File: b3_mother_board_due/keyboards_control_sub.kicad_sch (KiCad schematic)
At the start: 20 parts, among them J14 Upper Keyboard Left, J15 Upper Keyboard Right, J16 Lower Keyboard Left, J17 Lower Keyboard Right, U1 4051, U2 4051, U3 4051, U4 4051

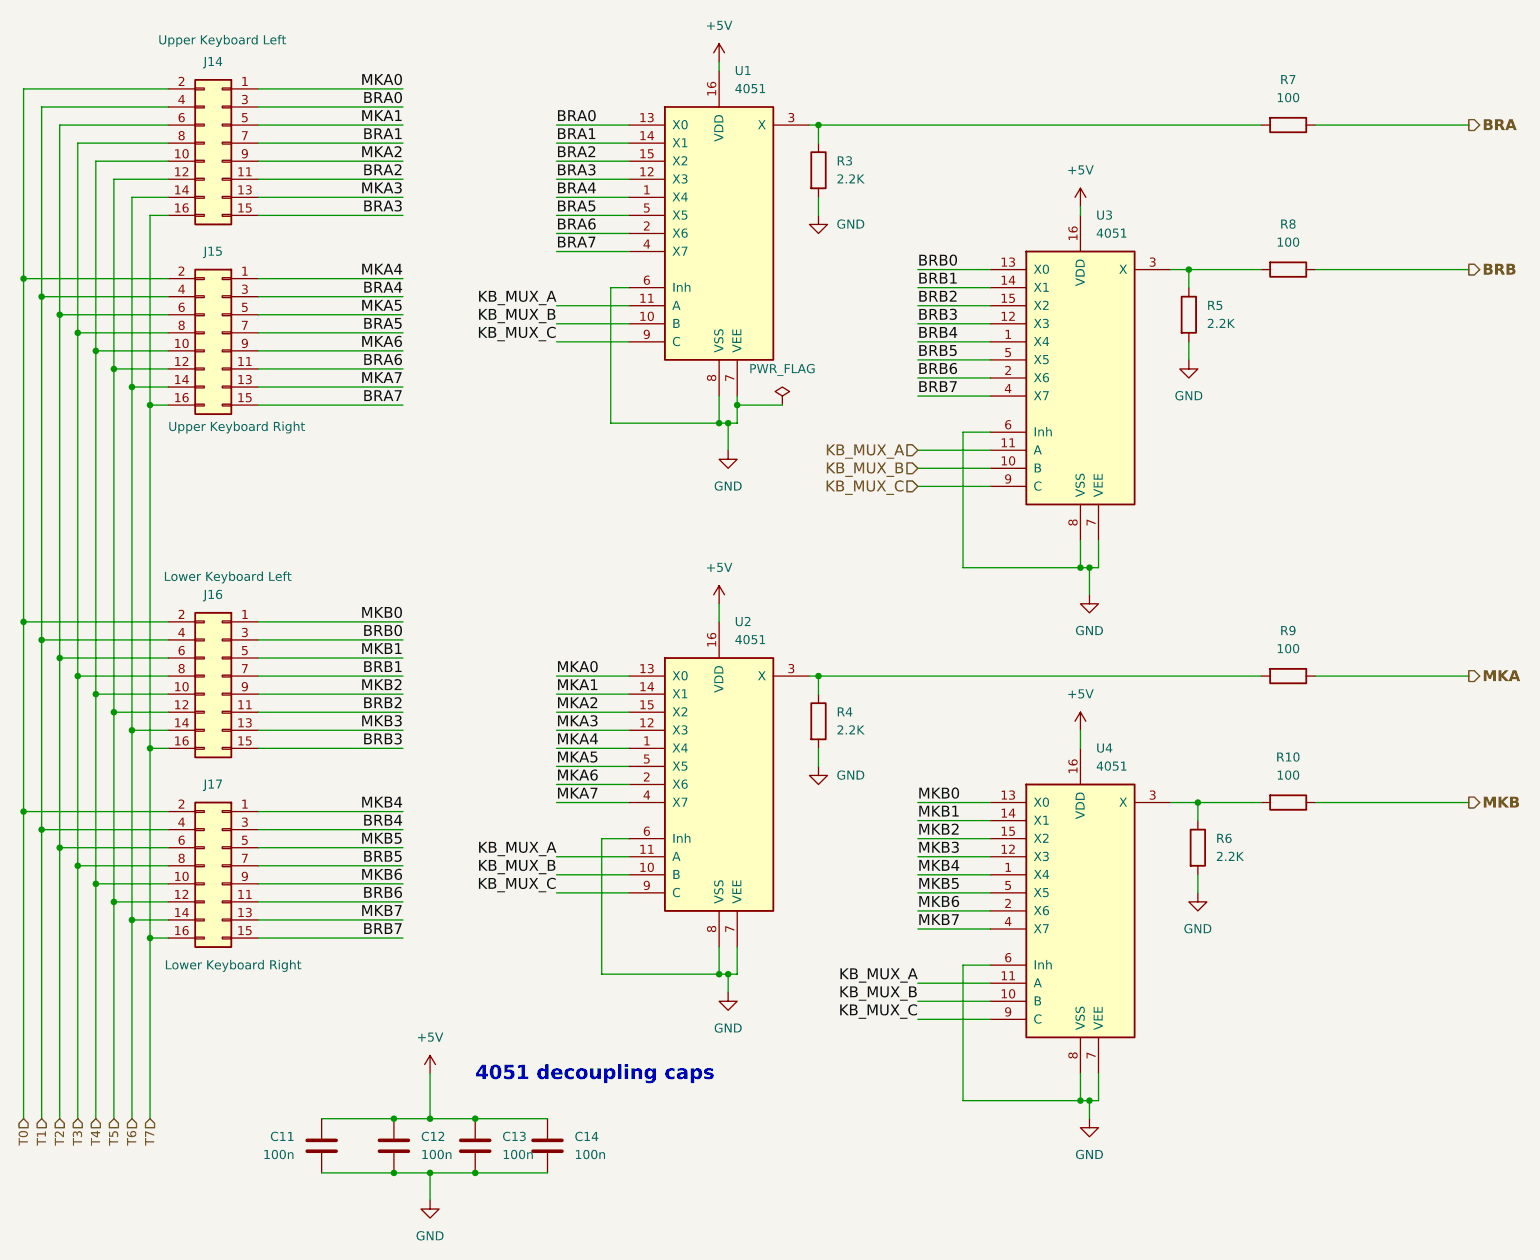
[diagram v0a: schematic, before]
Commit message: New organ architecture with mother board
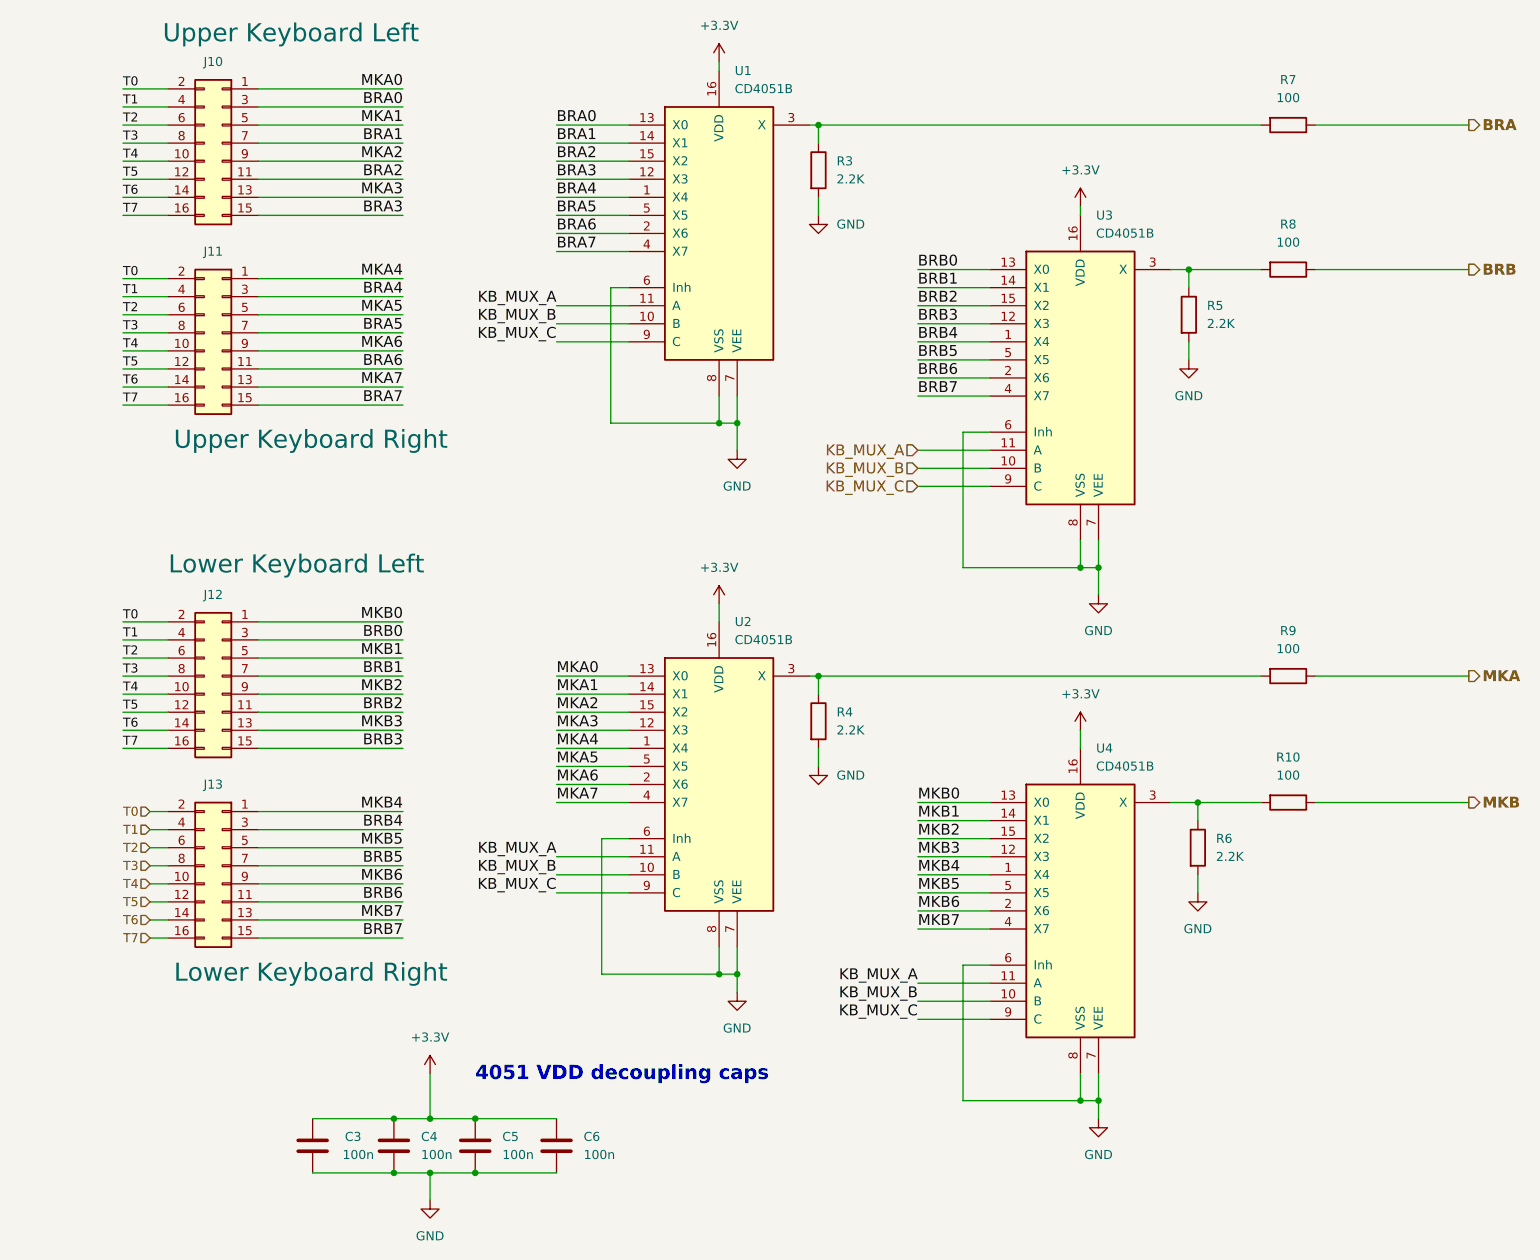
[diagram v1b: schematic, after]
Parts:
- U1, U2, U3, U4: value 4051 -> CD4051B
- renumbered C11 to C3, C12 to C4, C13 to C5, C14 to C6, J14 to J10, J15 to J11, J16 to J12, J17 to J13
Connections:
- net +5V renamed +3.3V
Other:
- note added: "4051 VDD decoupling caps"
- note removed: "4051 decoupling caps"
- title: Keyboards control -> Keyboards Matrix Scanner
- moved on the sheet: C3, C6
